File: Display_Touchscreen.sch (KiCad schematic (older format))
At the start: 7 parts, among them U1 TSC2007

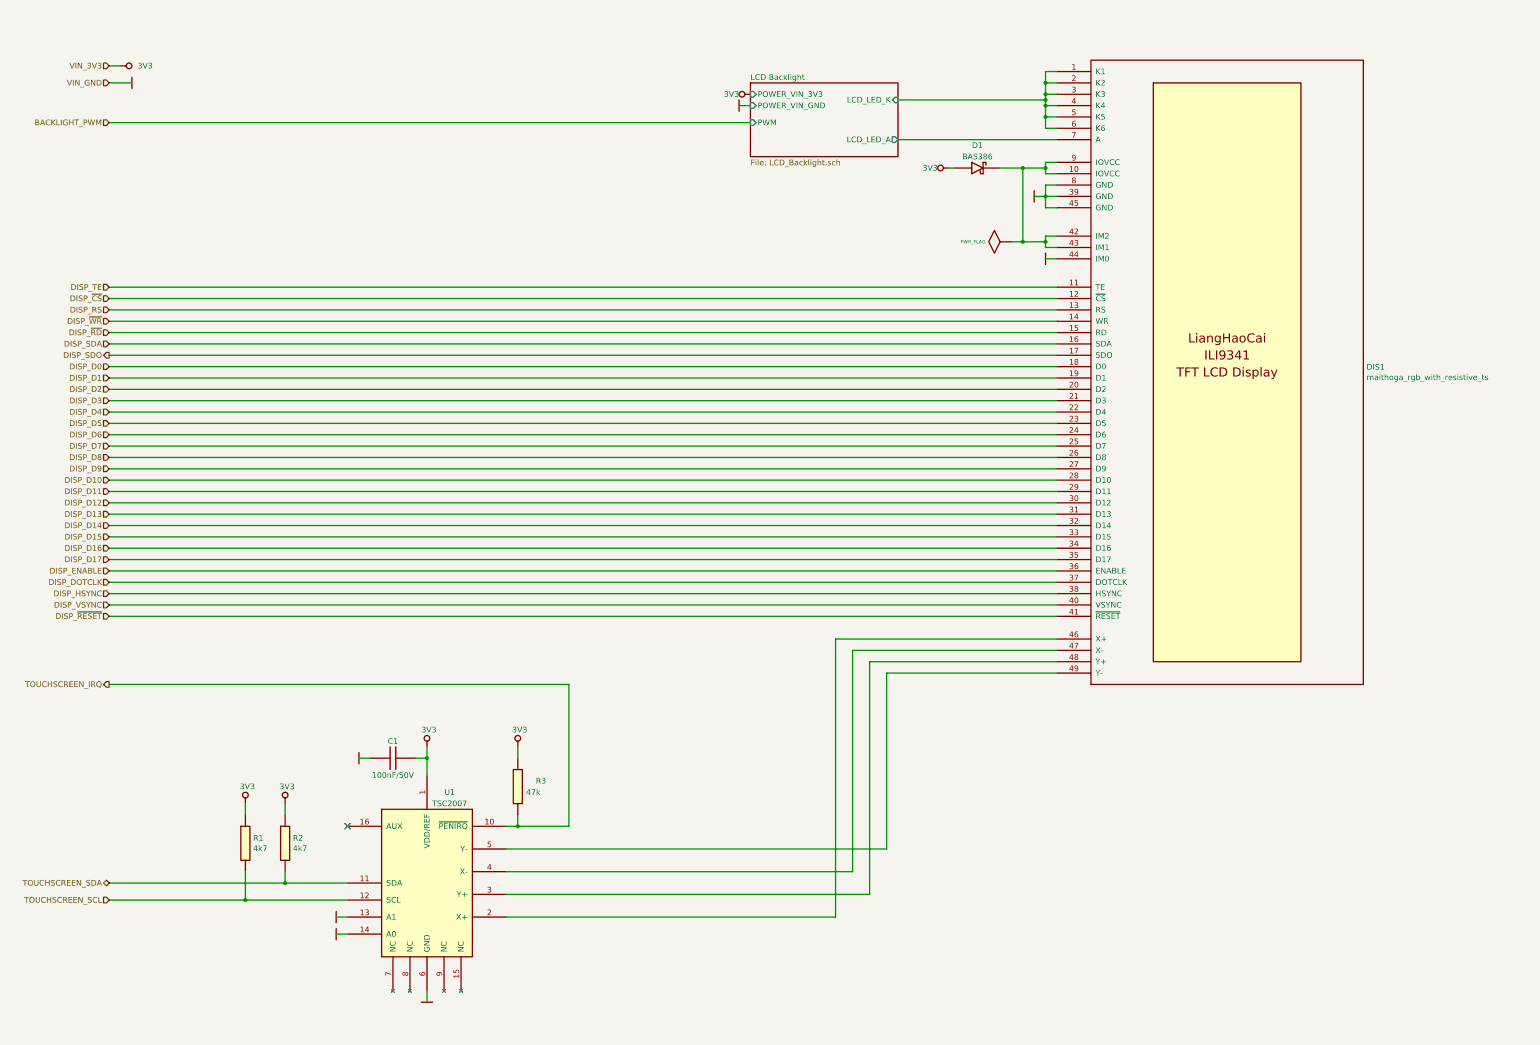
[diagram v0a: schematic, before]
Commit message: Filled hierarchical sheets
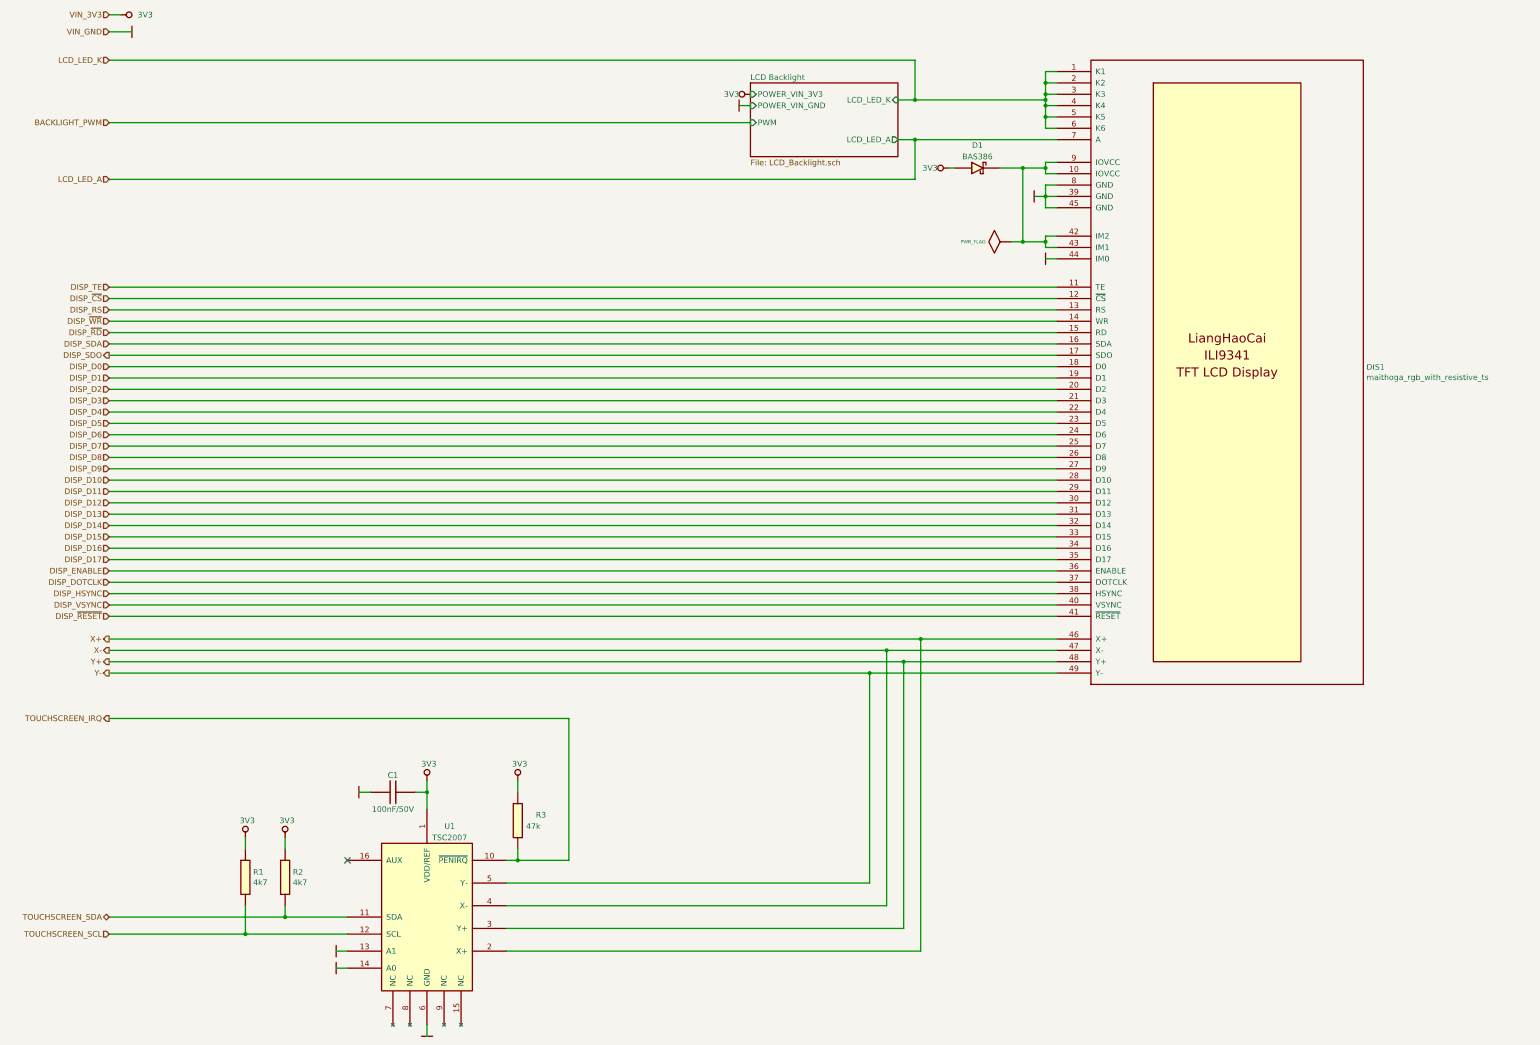
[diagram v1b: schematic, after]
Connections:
- net X+: now reaches DIS1.46 (X+), U1.2 (X+)
- net Y+: now reaches DIS1.48 (Y+), U1.3 (Y+)
- net X-: now reaches DIS1.47 (X-), U1.4 (X-)
- net Y-: now reaches DIS1.49 (Y-), U1.5 (Y-)
- net LCD Backlight/LCD_LED_A renamed LCD_LED_A
- net LCD Backlight/LCD_LED_K renamed LCD_LED_K
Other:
- moved on the sheet: C1, R1, R2, R3, U1

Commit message: Schematic ready, need check
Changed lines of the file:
@@
 Wire Wire Line
 	3500 4450 11850 4450
-Text HLabel 3500 4550 0    50   Input ~ 0
-DISP_SDA
 Wire Wire Line
 	3500 4550 11850 4550
-Text HLabel 3500 4650 0    50   Output ~ 0
+Text HLabel 3500 4650 0    50   Input ~ 0
 DISP_SDO
 Wire Wire Line
@@
 Text HLabel 3500 3100 0    50   Input ~ 0
 LCD_LED_A
+Text HLabel 3500 4550 0    50   Input ~ 0
+DISP_SDA
+$Comp
+L power:PWR_FLAG #FLG0101
+U 1 1 5F134E91
+P 11750 3350
+F 0 "#FLG0101" H 11750 3620 30  0001 C CNN
+F 1 "PWR_FLAG" H 11450 3450 30  0000 L CNN
+F 2 "" H 11750 3350 60  0000 C CNN
+F 3 "" H 11750 3350 60  0000 C CNN
+	1    11750 3350
+	-1   0    0    1
+$EndComp
+Connection ~ 11750 3350
 $EndSCHEMATC

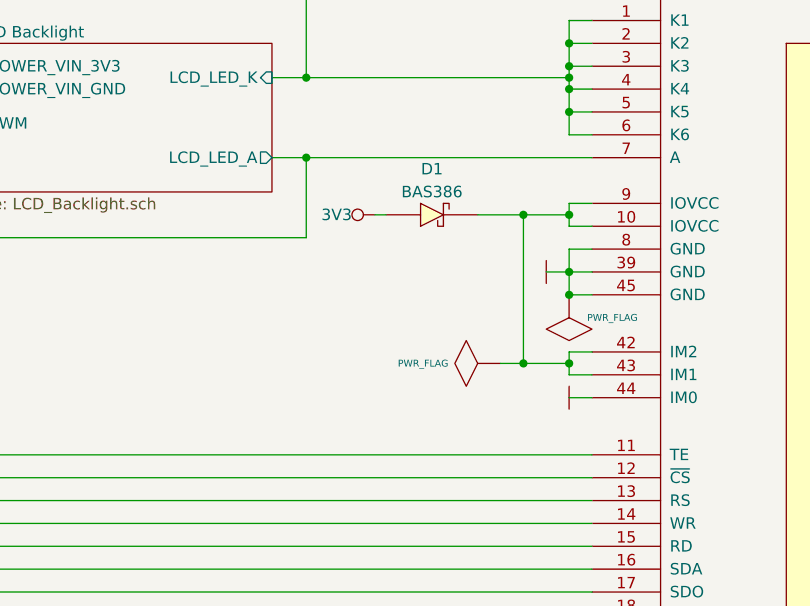
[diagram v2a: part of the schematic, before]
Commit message: Added resistor mode select on schematic
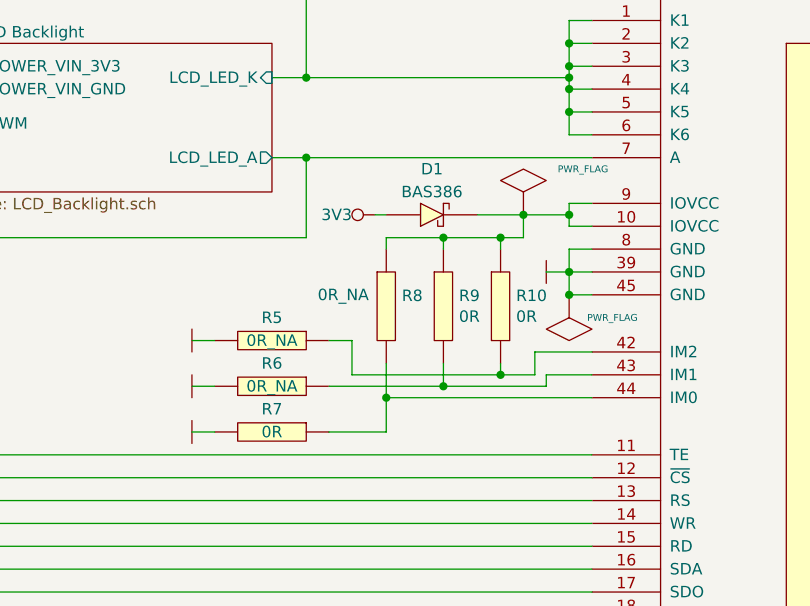
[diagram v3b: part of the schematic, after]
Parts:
- added R10, R7, R9: 0R, Resistor_Smd_0603:0R_0603, symbol Resistors_Smd0603:0R_0603
- added R5, R6, R8: 0R_NA, Resistor_Smd_0603:0R_0603, symbol Resistors_Smd0603:0R_0603
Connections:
- net GND: now also R5.2, R6.2, R7.2; no longer DIS1.44 (IM0)
- net at D1.2 (K), DIS1.10 (IOVCC), DIS1.9 (IOVCC): now also R10.1, R8.1, R9.1; no longer DIS1.42 (IM2), DIS1.43 (IM1)
- new net: DIS1.42 (IM2), R10.2, R5.1
- new net: DIS1.43 (IM1), R6.1, R9.2
- new net: DIS1.44 (IM0), R7.1, R8.2
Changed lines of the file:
@@
 Wire Wire Line
 	3500 6850 11850 6850
-Wire Wire Line
-	11750 3600 11850 3600
 $Comp
 L power:GND #PWR015
 U 1 1 5EF4B535
-P 11750 3800
-F 0 "#PWR015" H 11750 3900 30  0001 C CNN
-F 1 "GND" H 11750 3700 30  0001 C CNN
-F 2 "" H 11750 3800 60  0000 C CNN
-F 3 "" H 11750 3800 60  0000 C CNN
-	1    11750 3800
-	0    1    1    0
-$EndComp
-Wire Wire Line
-	11750 3800 11850 3800
+P 10100 3550
+F 0 "#PWR015" H 10100 3650 30  0001 C CNN
+F 1 "GND" H 10100 3450 30  0001 C CNN
+F 2 "" H 10100 3550 60  0000 C CNN
+F 3 "" H 10100 3550 60  0000 C CNN
+	1    10100 3550
+	0    1    1    0
+$EndComp
 Wire Wire Line
 	10450 2750 10600 2750
-Wire Wire Line
-	11750 3600 11750 3650
-Wire Wire Line
-	11750 3700 11850 3700
-Wire Wire Line
-	11350 3000 11550 3000
-Wire Wire Line
-	11750 3650 11550 3650
-Wire Wire Line
-	11550 3650 11550 3000
-Connection ~ 11750 3650
-Wire Wire Line
-	11750 3650 11750 3700
-Connection ~ 11550 3000
-Wire Wire Line
-	11550 3000 11750 3000
 Text HLabel 3500 6950 0    50   Input ~ 0
 DISP_~RESET~
@@
 L power:PWR_FLAG #FLG01
 U 1 1 5F160434
-P 11450 3650
-F 0 "#FLG01" H 11450 3920 30  0001 C CNN
-F 1 "PWR_FLAG" V 11450 3878 30  0000 L CNN
-F 2 "" H 11450 3650 60  0000 C CNN
-F 3 "" H 11450 3650 60  0000 C CNN
-	1    11450 3650
-	0    -1   -1   0
-$EndComp
-Wire Wire Line
-	11450 3650 11550 3650
-Connection ~ 11550 3650
+P 11550 3000
+F 0 "#FLG01" H 11550 3270 30  0001 C CNN
+F 1 "PWR_FLAG" H 11700 3200 30  0000 L CNN
+F 2 "" H 11550 3000 60  0000 C CNN
+F 3 "" H 11550 3000 60  0000 C CNN
+	1    11550 3000
+	1    0    0    -1
+$EndComp
 $Comp
 L Display_Lcd:maithoga_tft_480x320_rgb_with_resistive_ts DIS1
@@
 $EndComp
 Connection ~ 11750 3350
+$Comp
+L Resistors_Smd0603:0R_0603 R10
+U 1 1 5F075722
+P 11450 3400
+F 0 "R10" H 11518 3446 50  0000 L CNN
+F 1 "0R" H 11518 3355 50  0000 L CNN
+F 2 "Resistor_Smd_0603:0R_0603" H 11450 3400 60  0001 C CNN
+F 3 "Resistors/Smd_0603/Components_Documentation/Vishay_Resistors_SM0603.pdf" H 11450 3400 60  0001 C CNN
+F 4 "ROYAL OHM" H 11450 3400 50  0001 C CNN "Manufacturer"
+F 5 "0603SAJ0000T5E" H 11450 3400 50  0001 C CNN "Manufacturer Part Number"
+F 6 "TME" H 11450 3400 50  0001 C CNN "Supplier"
+F 7 "SMD0603-0R" H 11450 3400 50  0001 C CNN "Supplier Part Number"
+F 8 "https://www.tme.eu/pl/details/smd0603-0r/rezystory-smd-0603/royal-ohm/0603saj0000t5e/" H 11450 3400 50  0001 C CNN "URL"
+F 9 "0,03966" H 11450 3400 50  0001 C CNN "Price@1pc"
+F 10 "0,00967" H 11450 3400 50  0001 C CNN "Price@1000pcs"
+F 11 "0603" H 11450 3400 50  0001 C CNN "Package"
+	1    11450 3400
+	1    0    0    -1
+$EndComp
+$Comp
+L Resistors_Smd0603:0R_0603 R9
+U 1 1 5F077563
+P 11200 3400
+F 0 "R9" H 11268 3446 50  0000 L CNN
+F 1 "0R" H 11268 3355 50  0000 L CNN
+F 2 "Resistor_Smd_0603:0R_0603" H 11200 3400 60  0001 C CNN
+F 3 "Resistors/Smd_0603/Components_Documentation/Vishay_Resistors_SM0603.pdf" H 11200 3400 60  0001 C CNN
+F 4 "ROYAL OHM" H 11200 3400 50  0001 C CNN "Manufacturer"
+F 5 "0603SAJ0000T5E" H 11200 3400 50  0001 C CNN "Manufacturer Part Number"
+F 6 "TME" H 11200 3400 50  0001 C CNN "Supplier"
+F 7 "SMD0603-0R" H 11200 3400 50  0001 C CNN "Supplier Part Number"
+F 8 "https://www.tme.eu/pl/details/smd0603-0r/rezystory-smd-0603/royal-ohm/0603saj0000t5e/" H 11200 3400 50  0001 C CNN "URL"
+F 9 "0,03966" H 11200 3400 50  0001 C CNN "Price@1pc"
+F 10 "0,00967" H 11200 3400 50  0001 C CNN "Price@1000pcs"
+F 11 "0603" H 11200 3400 50  0001 C CNN "Package"
+	1    11200 3400
+	1    0    0    -1
+$EndComp
+$Comp
+L Resistors_Smd0603:0R_0603 R8
+U 1 1 5F07DB90
+P 10950 3400
+F 0 "R8" H 11018 3446 50  0000 L CNN
+F 1 "0R_NA" H 10650 3450 50  0000 L CNN
+F 2 "Resistor_Smd_0603:0R_0603" H 10950 3400 60  0001 C CNN
+F 3 "Resistors/Smd_0603/Components_Documentation/Vishay_Resistors_SM0603.pdf" H 10950 3400 60  0001 C CNN
+F 4 "ROYAL OHM" H 10950 3400 50  0001 C CNN "Manufacturer"
+F 5 "0603SAJ0000T5E" H 10950 3400 50  0001 C CNN "Manufacturer Part Number"
+F 6 "TME" H 10950 3400 50  0001 C CNN "Supplier"
+F 7 "SMD0603-0R" H 10950 3400 50  0001 C CNN "Supplier Part Number"
+F 8 "https://www.tme.eu/pl/details/smd0603-0r/rezystory-smd-0603/royal-ohm/0603saj0000t5e/" H 10950 3400 50  0001 C CNN "URL"
+F 9 "0,03966" H 10950 3400 50  0001 C CNN "Price@1pc"
+F 10 "0,00967" H 10950 3400 50  0001 C CNN "Price@1000pcs"
+F 11 "0603" H 10950 3400 50  0001 C CNN "Package"
+	1    10950 3400
+	1    0    0    -1
+$EndComp
+Wire Wire Line
+	11350 3000 11550 3000
+Connection ~ 11550 3000
+Wire Wire Line
+	11550 3000 11750 3000
+Wire Wire Line
+	11850 3600 11600 3600
+Wire Wire Line
+	11600 3600 11600 3700
+Wire Wire Line
+	11600 3700 11450 3700
+Wire Wire Line
+	11450 3700 11450 3650
+Wire Wire Line
+	11850 3700 11650 3700
+Wire Wire Line
+	11650 3700 11650 3750
+Wire Wire Line
+	11650 3750 11200 3750
+Wire Wire Line
+	11200 3750 11200 3650
+Wire Wire Line
+	11850 3800 10950 3800
+Wire Wire Line
+	10950 3800 10950 3650
+$Comp
+L Resistors_Smd0603:0R_0603 R7
+U 1 1 5F0A0296
+P 10450 3950
+F 0 "R7" V 10350 3950 50  0000 C CNN
+F 1 "0R" V 10450 3950 50  0000 C CNN
+F 2 "Resistor_Smd_0603:0R_0603" H 10450 3950 60  0001 C CNN
+F 3 "Resistors/Smd_0603/Components_Documentation/Vishay_Resistors_SM0603.pdf" H 10450 3950 60  0001 C CNN
+F 4 "ROYAL OHM" H 10450 3950 50  0001 C CNN "Manufacturer"
+F 5 "0603SAJ0000T5E" H 10450 3950 50  0001 C CNN "Manufacturer Part Number"
+F 6 "TME" H 10450 3950 50  0001 C CNN "Supplier"
+F 7 "SMD0603-0R" H 10450 3950 50  0001 C CNN "Supplier Part Number"
+F 8 "https://www.tme.eu/pl/details/smd0603-0r/rezystory-smd-0603/royal-ohm/0603saj0000t5e/" H 10450 3950 50  0001 C CNN "URL"
+F 9 "0,03966" H 10450 3950 50  0001 C CNN "Price@1pc"
+F 10 "0,00967" H 10450 3950 50  0001 C CNN "Price@1000pcs"
+F 11 "0603" H 10450 3950 50  0001 C CNN "Package"
+	1    10450 3950
+	0    1    1    0
+$EndComp
+$Comp
+L Resistors_Smd0603:0R_0603 R6
+U 1 1 5F0A15D6
+P 10450 3750
+F 0 "R6" V 10350 3750 50  0000 C CNN
+F 1 "0R_NA" V 10450 3750 50  0000 C CNN
+F 2 "Resistor_Smd_0603:0R_0603" H 10450 3750 60  0001 C CNN
+F 3 "Resistors/Smd_0603/Components_Documentation/Vishay_Resistors_SM0603.pdf" H 10450 3750 60  0001 C CNN
+F 4 "ROYAL OHM" H 10450 3750 50  0001 C CNN "Manufacturer"
+F 5 "0603SAJ0000T5E" H 10450 3750 50  0001 C CNN "Manufacturer Part Number"
+F 6 "TME" H 10450 3750 50  0001 C CNN "Supplier"
+F 7 "SMD0603-0R" H 10450 3750 50  0001 C CNN "Supplier Part Number"
+F 8 "https://www.tme.eu/pl/details/smd0603-0r/rezystory-smd-0603/royal-ohm/0603saj0000t5e/" H 10450 3750 50  0001 C CNN "URL"
+F 9 "0,03966" H 10450 3750 50  0001 C CNN "Price@1pc"
+F 10 "0,00967" H 10450 3750 50  0001 C CNN "Price@1000pcs"
+F 11 "0603" H 10450 3750 50  0001 C CNN "Package"
+	1    10450 3750
+	0    1    1    0
+$EndComp
+$Comp
+L Resistors_Smd0603:0R_0603 R5
+U 1 1 5F0A7246
+P 10450 3550
+F 0 "R5" V 10350 3550 50  0000 C CNN
+F 1 "0R_NA" V 10450 3550 50  0000 C CNN
+F 2 "Resistor_Smd_0603:0R_0603" H 10450 3550 60  0001 C CNN
+F 3 "Resistors/Smd_0603/Components_Documentation/Vishay_Resistors_SM0603.pdf" H 10450 3550 60  0001 C CNN
+F 4 "ROYAL OHM" H 10450 3550 50  0001 C CNN "Manufacturer"
+F 5 "0603SAJ0000T5E" H 10450 3550 50  0001 C CNN "Manufacturer Part Number"
+F 6 "TME" H 10450 3550 50  0001 C CNN "Supplier"
+F 7 "SMD0603-0R" H 10450 3550 50  0001 C CNN "Supplier Part Number"
+F 8 "https://www.tme.eu/pl/details/smd0603-0r/rezystory-smd-0603/royal-ohm/0603saj0000t5e/" H 10450 3550 50  0001 C CNN "URL"
+F 9 "0,03966" H 10450 3550 50  0001 C CNN "Price@1pc"
+F 10 "0,00967" H 10450 3550 50  0001 C CNN "Price@1000pcs"
+F 11 "0603" H 10450 3550 50  0001 C CNN "Package"
+	1    10450 3550
+	0    1    1    0
+$EndComp
+Wire Wire Line
+	10950 3800 10950 3950
+Wire Wire Line
+	10950 3950 10700 3950
+Connection ~ 10950 3800
+Wire Wire Line
+	11200 3750 10700 3750
+Connection ~ 11200 3750
+$Comp
+L power:GND #PWR0111
+U 1 1 5F0BE62E
+P 10100 3950
+F 0 "#PWR0111" H 10100 4050 30  0001 C CNN
+F 1 "GND" H 10100 3850 30  0001 C CNN
+F 2 "" H 10100 3950 60  0000 C CNN
+F 3 "" H 10100 3950 60  0000 C CNN
+	1    10100 3950
+	0    1    1    0
+$EndComp
+$Comp
+L power:GND #PWR0112
+U 1 1 5F0C5042
+P 10100 3750
+F 0 "#PWR0112" H 10100 3850 30  0001 C CNN
+F 1 "GND" H 10100 3650 30  0001 C CNN
+F 2 "" H 10100 3750 60  0000 C CNN
+F 3 "" H 10100 3750 60  0000 C CNN
+	1    10100 3750
+	0    1    1    0
+$EndComp
+Wire Wire Line
+	10200 3950 10100 3950
+Wire Wire Line
+	10200 3750 10100 3750
+Wire Wire Line
+	10200 3550 10100 3550
+Wire Wire Line
+	11450 3700 10800 3700
+Wire Wire Line
+	10800 3700 10800 3550
+Wire Wire Line
+	10800 3550 10700 3550
+Connection ~ 11450 3700
+Wire Wire Line
+	10950 3150 10950 3100
+Wire Wire Line
+	10950 3100 11200 3100
+Wire Wire Line
+	11450 3100 11450 3150
+Wire Wire Line
+	11200 3150 11200 3100
+Connection ~ 11200 3100
+Wire Wire Line
+	11200 3100 11450 3100
+Wire Wire Line
+	11550 3000 11550 3100
+Wire Wire Line
+	11550 3100 11450 3100
+Connection ~ 11450 3100
 $EndSCHEMATC
